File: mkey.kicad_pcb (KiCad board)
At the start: 2 copper layers, 346.2 x 95.5 mm, 168 parts, among them J1 USB_C_REP_2.0, J2 24 pin LCD FPC connector, U1 ESP32-S3-WROOM-1, U2 SY8088

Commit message: Switch to m2 mounting holes
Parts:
- removed the ? at (272.3, 108.7)
- removed the ? at (57.1, 122.2)
- removed the ? at (158.8, 100.8)
- removed the ? at (60.3, 70.6)
- removed the REF** at (377.0, 49.2)
- added ?: , , F.Cu at (39.8, 136.4)
- added ?: , , F.Cu at (81.6, 82.3)
- added ?: , , F.Cu at (372.2, 112.0)
- added ?: , , F.Cu at (233.7, 82.5)
- added REF**: MountingHole_2.2mm_M2_Pad, MountingHole:MountingHole_2.2mm_M2_Pad, F.Cu at (377.3, 48.2)
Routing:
- net USB_D-: track 39.3 -> 38.5 mm
- net GND: vias 12 -> 25

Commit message: vias, vias everywhere
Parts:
- renumbered BOOT to BOOT_SW1, RESET to RESET_SW1
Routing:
- net GND: vias 25 -> 149

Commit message: update switch annotations
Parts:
- renumbered RESET_SW1 to SW0, BOOT_SW1 to SW1
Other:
- board text added: "BOOT"
- board text added: "RESET"
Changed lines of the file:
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@@
     (fp_arc (start -46.63125 7.500001) (mid -46.777697 7.853554) (end -47.13125 8.000001)
       (stroke (width 0.05) (type solid)) (layer "Eco2.User"))
-    (fp_arc (start 46.63125 -5.499999) (mid 46.777693 -5.853571) (end 47.13125 -5.999999)
+    (fp_arc (start 46.63125 -5.499999) (mid 46.777699 -5.853535) (end 47.13125 -5.999999)
       (stroke (width 0.05) (type solid)) (layer "Eco2.User"))
-    (fp_arc (start 47.13125 8.000001) (mid 46.777729 7.853537) (end 46.63125 7.500001)
+    (fp_arc (start 47.13125 8.000001) (mid 46.777693 7.853543) (end 46.63125 7.500001)
       (stroke (width 0.05) (type solid)) (layer "Eco2.User"))
-    (fp_arc (start 52.880039 -5.999999) (mid 53.233567 -5.853539) (end 53.380039 -5.499999)
+    (fp_arc (start 52.880039 -5.999999) (mid 53.233602 -5.853545) (end 53.380039 -5.499999)
       (stroke (width 0.05) (type solid)) (layer "Eco2.User"))
-    (fp_arc (start 53.38125 7.500001) (mid 53.234806 7.853571) (end 52.88125 8.000001)
+    (fp_arc (start 53.38125 7.500001) (mid 53.2348 7.853536) (end 52.88125 8.000001)
       (stroke (width 0.05) (type solid)) (layer "Eco2.User"))
     (pad "" thru_hole circle (at -50.00625 -6.985 180) (size 4 4) (drill 3.048) (layers "*.Cu" "B.Mask"))
@@
     (fp_arc (start 8.53125 -5.499999) (mid 8.677685 -5.853565) (end 9.03125 -5.999999)
       (stroke (width 0.05) (type solid)) (layer "Eco2.User"))
-    (fp_arc (start 9.03125 8.000001) (mid 8.677729 7.853537) (end 8.53125 7.500001)
+    (fp_arc (start 9.03125 8.000001) (mid 8.677693 7.853543) (end 8.53125 7.500001)
       (stroke (width 0.05) (type solid)) (layer "Eco2.User"))
-    (fp_arc (start 14.780039 -5.999999) (mid 15.133567 -5.853539) (end 15.280039 -5.499999)
+    (fp_arc (start 14.780039 -5.999999) (mid 15.133602 -5.853545) (end 15.280039 -5.499999)
       (stroke (width 0.05) (type solid)) (layer "Eco2.User"))
-    (fp_arc (start 15.28125 7.500001) (mid 15.134806 7.853571) (end 14.78125 8.000001)
+    (fp_arc (start 15.28125 7.500001) (mid 15.1348 7.853536) (end 14.78125 8.000001)
       (stroke (width 0.05) (type solid)) (layer "Eco2.User"))
     (pad "" thru_hole circle (at -11.90625 -6.985) (size 4 4) (drill 3.048) (layers "*.Cu" "B.Mask"))
@@
     (fp_arc (start 8.53125 -5.499999) (mid 8.677685 -5.853565) (end 9.03125 -5.999999)
       (stroke (width 0.05) (type solid)) (layer "Eco2.User"))
-    (fp_arc (start 9.03125 8.000001) (mid 8.677729 7.853537) (end 8.53125 7.500001)
+    (fp_arc (start 9.03125 8.000001) (mid 8.677693 7.853543) (end 8.53125 7.500001)
       (stroke (width 0.05) (type solid)) (layer "Eco2.User"))
-    (fp_arc (start 14.780039 -5.999999) (mid 15.133567 -5.853539) (end 15.280039 -5.499999)
+    (fp_arc (start 14.780039 -5.999999) (mid 15.133602 -5.853545) (end 15.280039 -5.499999)
       (stroke (width 0.05) (type solid)) (layer "Eco2.User"))
-    (fp_arc (start 15.28125 7.500001) (mid 15.134806 7.853571) (end 14.78125 8.000001)
+    (fp_arc (start 15.28125 7.500001) (mid 15.1348 7.853536) (end 14.78125 8.000001)
       (stroke (width 0.05) (type solid)) (layer "Eco2.User"))
     (pad "" thru_hole circle (at -11.90625 -6.985) (size 4 4) (drill 3.048) (layers "*.Cu" "B.Mask"))
@@
     (property "ki_keywords" "switch normally-open pushbutton push-button")
     (attr smd)
-    (fp_text reference "RESET_SW1" (at 0 -2.72325) (layer "B.SilkS")
+    (fp_text reference "SW0" (at 3.57367 -0.548537 90) (layer "B.SilkS")
         (effects (font (size 1 1) (thickness 0.15)) (justify mirror))
     )
@@
     (property "ki_keywords" "capacitor cap")
     (attr smd)
-    (fp_text reference "C4" (at 2.82619 0 90) (layer "B.SilkS")
+    (fp_text reference "C4" (at -2.884895 0.027878 90) (layer "B.SilkS")
         (effects (font (size 1 1) (thickness 0.15)) (justify mirror))
     )
@@
     (property "ki_keywords" "switch normally-open pushbutton push-button")
     (attr smd)
-    (fp_text reference "BOOT_SW1" (at -0.01875 -2.8075 90) (layer "B.SilkS")
+    (fp_text reference "SW1" (at -3.97875 -0.0275 180) (layer "B.SilkS")
         (effects (font (size 1 1) (thickness 0.15)) (justify mirror))
     )
@@
     (property "ki_keywords" "capacitor cap")
     (attr smd)
-    (fp_text reference "C3" (at 5.10619 1 90) (layer "B.SilkS")
+    (fp_text reference "C3" (at 2.403855 1.009128 90) (layer "B.SilkS")
         (effects (font (size 1 1) (thickness 0.15)) (justify mirror))
     )
@@
   (gr_rect (start 34.89 44.74) (end 381.04 140.21)
     (stroke (width 0.1) (type default)) (fill none) (layer "Edge.Cuts"))
+  (gr_text "RESET" (at 352.41 60.52) (layer "B.SilkS")
+    (effects (font (size 1 1) (thickness 0.15)) (justify left bottom mirror))
+  )
+  (gr_text "BOOT" (at 302.86 74.22 -90) (layer "B.SilkS")
+    (effects (font (size 1 1) (thickness 0.15)) (justify left bottom mirror))
+  )
   (segment (start 325.4375 53.975) (end 334.16875 53.975) (width 0.25) (layer "F.Cu") (net 1))
   (segment (start 341.888279 50.066886) (end 342.713031 50.066886) (width 0.5) (layer "F.Cu") (net 1))

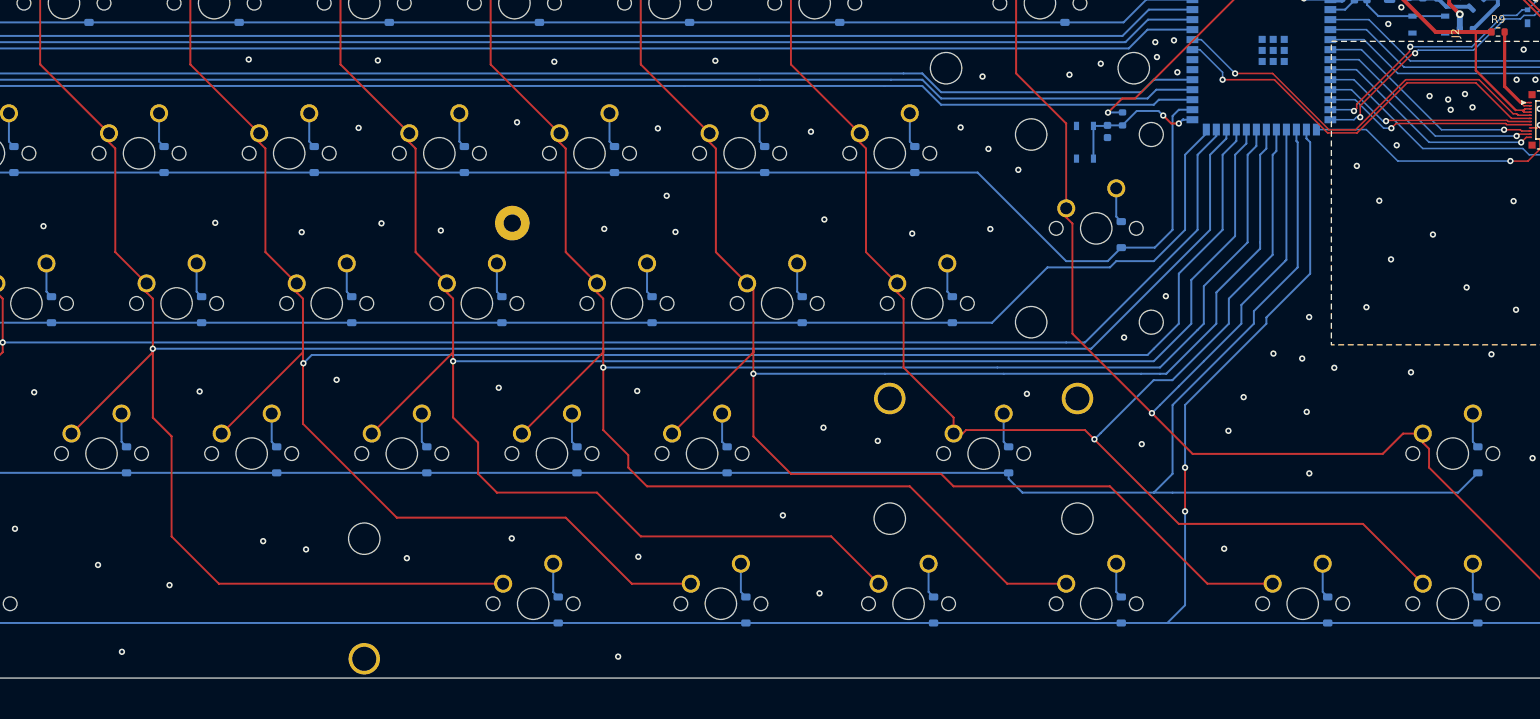
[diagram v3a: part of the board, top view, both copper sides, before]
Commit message: Add silkscreen artwork
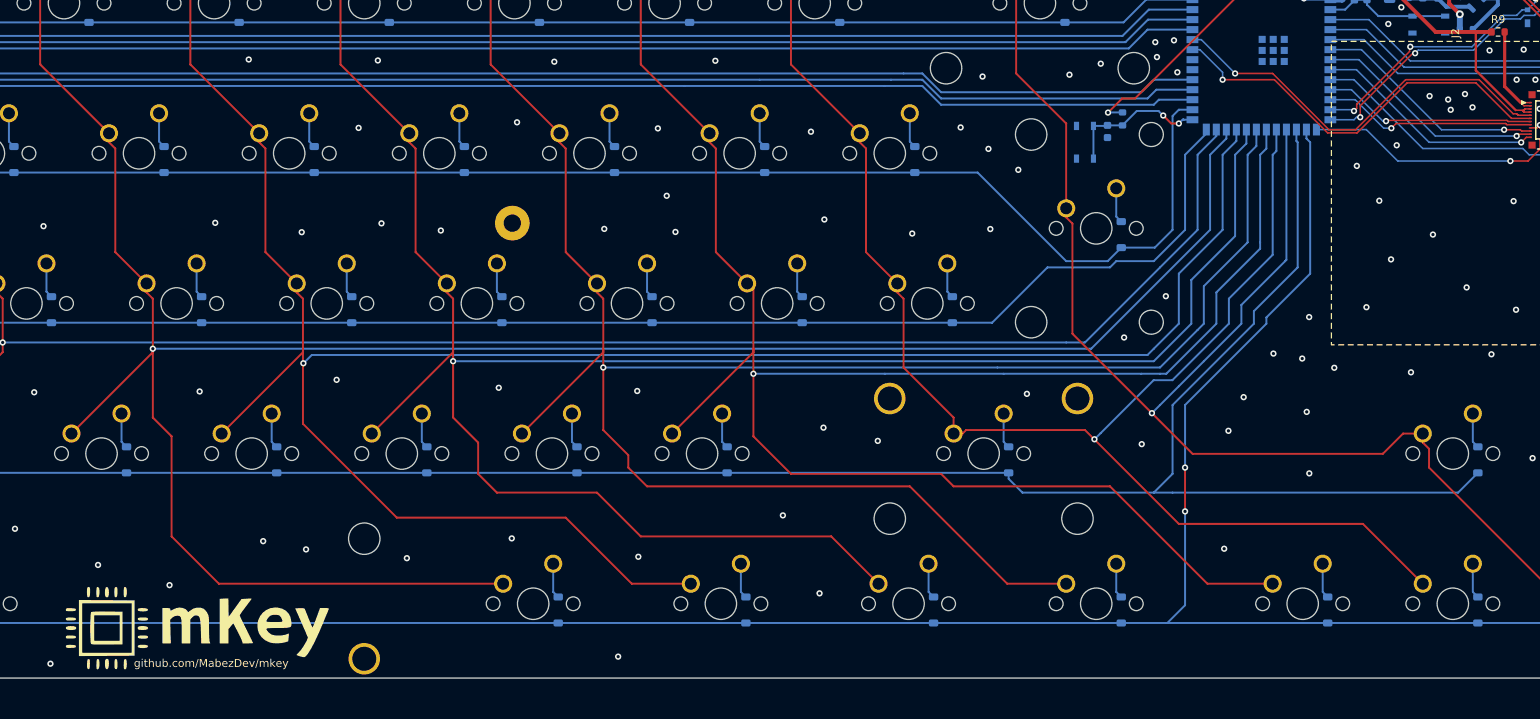
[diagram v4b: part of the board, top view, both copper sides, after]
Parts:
- added G***: LOGO, GRAPHICS:mkey, F.Cu at (193.8, 133.9)
- added G***: LOGO, GRAPHICS:mkey, B.Cu at (361.8, 67.5)
- added G***: LOGO, GRAPHICS:qr, B.Cu at (355.4, 88.9)
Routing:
- net GND: vias 149 -> 150
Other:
- board text added: "github.com/MabezDev/mkey"
- board text added: "v1.0 © Scott Mabin 2024"
